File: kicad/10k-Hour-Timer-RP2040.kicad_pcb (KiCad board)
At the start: 2 copper layers, 2 parts, among them J1 USB_C_Receptacle_USB2.0_16P, J2 Conn_01x03_MountingPin

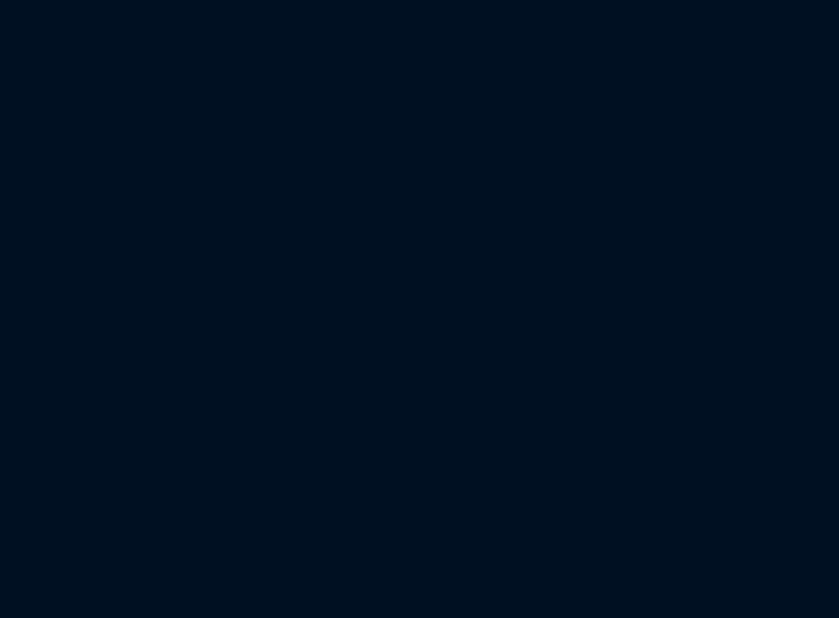
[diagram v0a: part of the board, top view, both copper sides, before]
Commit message: 3d model imports
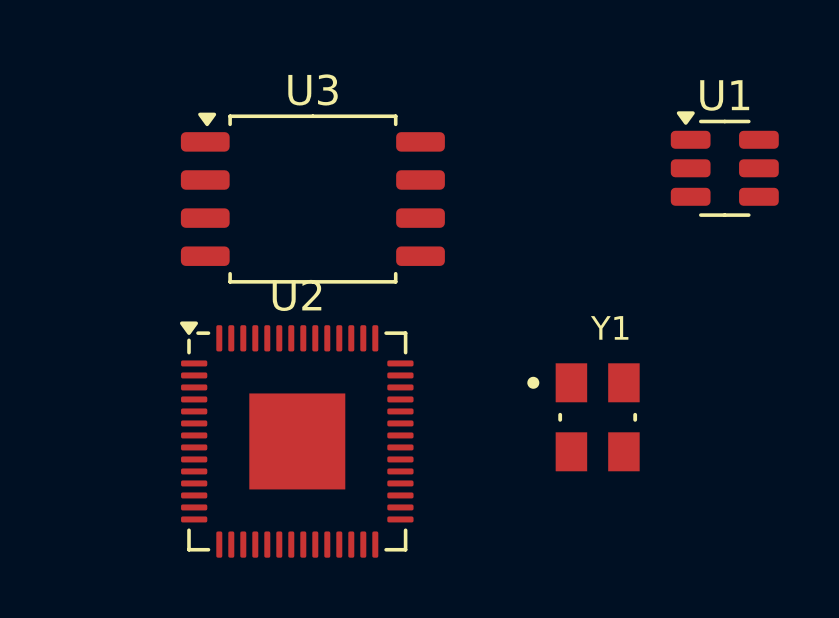
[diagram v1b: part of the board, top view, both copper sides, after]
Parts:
- added U1: USBLC6-2SC6, Package_TO_SOT_SMD:SOT-23-6, F.Cu at (133.9, 34.0)
- added U2: RP2040, Package_DFN_QFN:QFN-56-1EP_7x7mm_P0.4mm_EP3.2x3.2mm, F.Cu at (119.6, 43.2)
- added U3: W25Q128JVS, Package_SO:SOIC-8_5.3x5.3mm_P1.27mm, F.Cu at (120.1, 35.1)
- added Y1: ABM8-272-T3, project footprints:XTAL_ABM8-272-T3, F.Cu at (129.6, 42.4)
- J1: footprint Connector_USB:USB_C_Receptacle_JAE_DX07S016JA1R1500 -> project footprints:USB_C_Receptacle_JAE_DX07S016JA1R1500
- J2: footprint Connector_JST:JST_SH_SM03B-SRSS-TB_1x03-1MP_P1.00mm_Horizontal -> project footprints:JST_SH_SM03B-SRSS-TB_1x03-1MP_P1.00mm_Horizontal
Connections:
- net Net-(J1-VBUS-PadA4) renamed /01-04-Power-DCDC-Charger-Battery/5V_USB
- J1 pad A1: Net-(J1-GND-PadA1) -> GND
- J1 pad A12: Net-(J1-GND-PadA1) -> GND
- J1 pad A5: unconnected-(J1-CC1-PadA5) -> Net-(J1-CC1)
- J1 pad A6: unconnected-(J1-D+-PadA6) -> /USB_In_D+
- J1 pad A7: unconnected-(J1-D--PadA7) -> /USB_In_D-
- J1 pad B1: Net-(J1-GND-PadA1) -> GND
- J1 pad B12: Net-(J1-GND-PadA1) -> GND
- J1 pad B5: unconnected-(J1-CC2-PadB5) -> Net-(J1-CC2)
- J1 pad B6: unconnected-(J1-D+-PadB6) -> /USB_In_D+
- J1 pad B7: unconnected-(J1-D--PadB7) -> /USB_In_D-
- J1 pad S1: unconnected-(J1-SHIELD-PadS1) -> Net-(J1-SHIELD)
- J2 pad 1: unconnected-(J2-Pin_1-Pad1) -> /SWCK_UART_Rx
- J2 pad 2: unconnected-(J2-Pin_2-Pad2) -> GND
- J2 pad 3: unconnected-(J2-Pin_3-Pad3) -> /SWD_UART_Tx

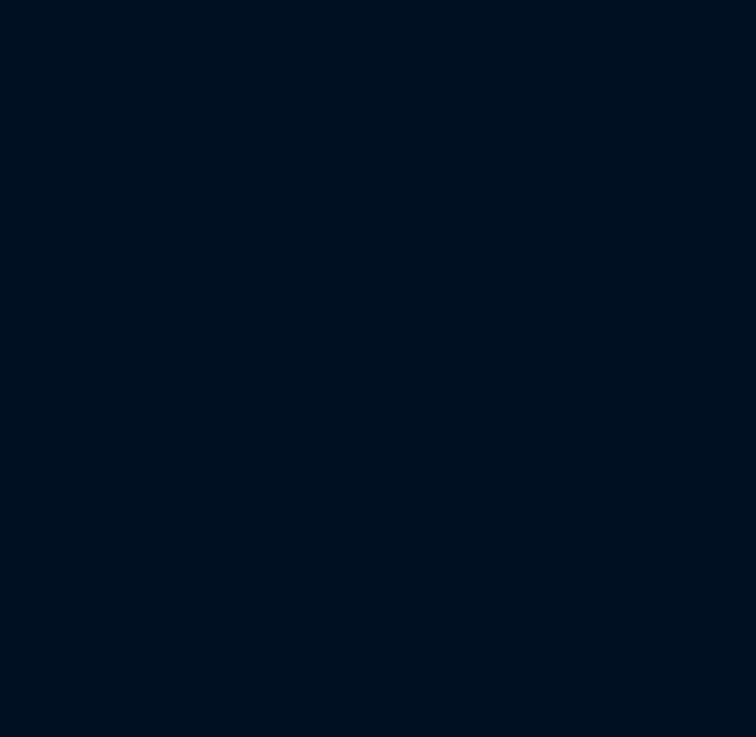
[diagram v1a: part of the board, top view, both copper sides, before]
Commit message: added charger and power mux
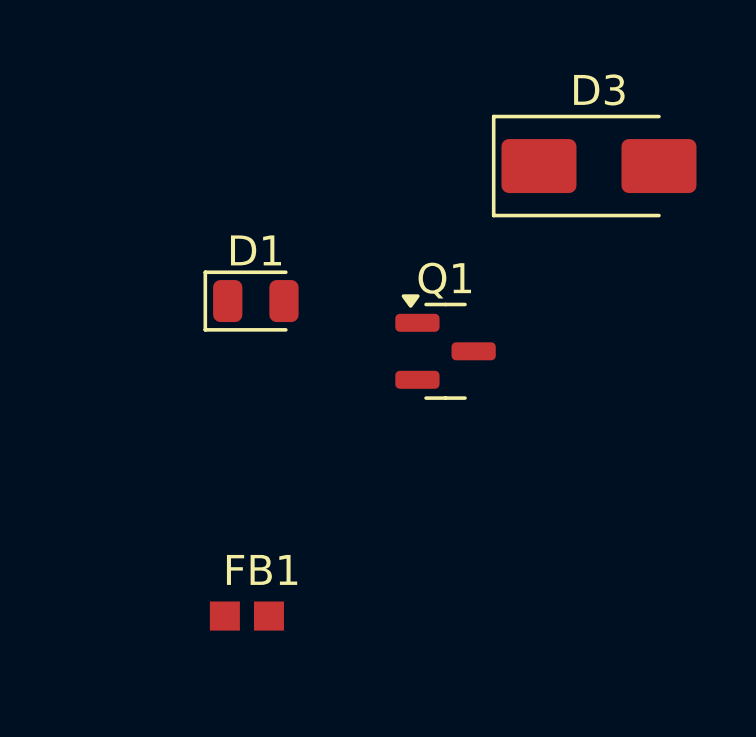
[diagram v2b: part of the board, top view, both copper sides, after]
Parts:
- added D1: LED, LED_SMD:LED_0805_2012Metric, F.Cu at (154.6, 34.5)
- added D3: SS14, Diode_SMD:D_SMA, F.Cu at (166.0, 30.0)
- added FB1: BLM18SP221SN1D, project footprints:BLM18SP221SN1D_BEADC1608X95N, F.Cu at (154.3, 45.0)
- added Q1: PMOS, Package_TO_SOT_SMD:SOT-23, F.Cu at (160.9, 36.2)
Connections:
- net /01-04-Power-DCDC-Charger-Battery/5V_USB renamed Net-(U1-VBUS)

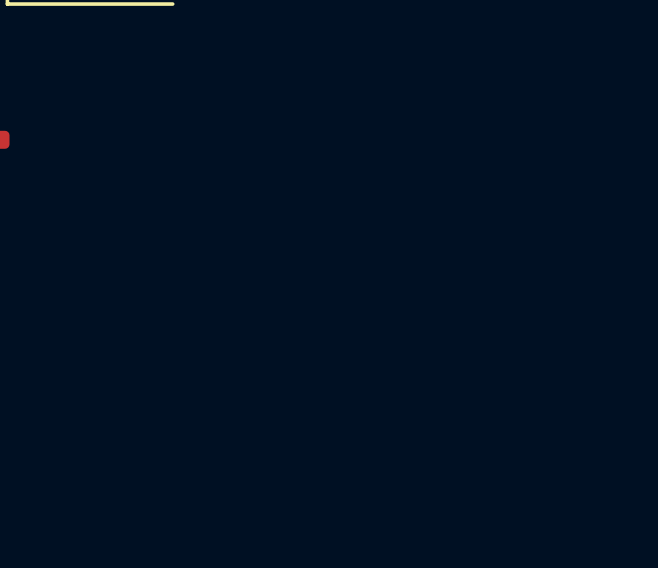
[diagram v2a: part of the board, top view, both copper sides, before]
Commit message: battery charger and protection
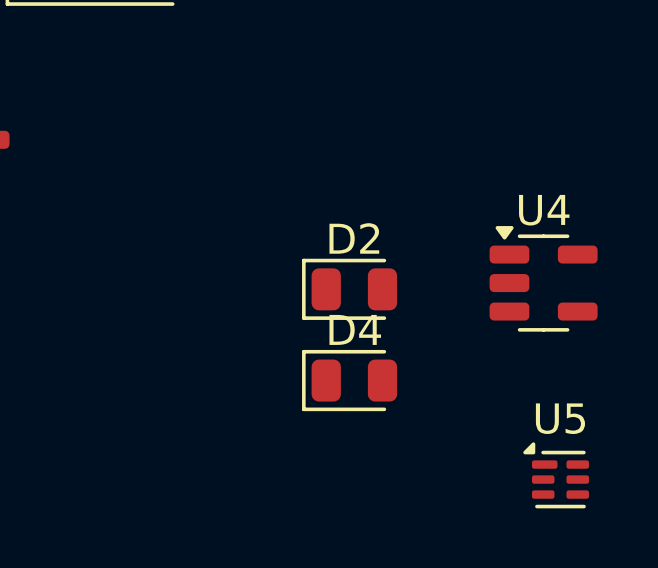
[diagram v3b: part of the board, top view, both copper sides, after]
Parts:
- added D2: BATT, LED_SMD:LED_0805_2012Metric, F.Cu at (174.1, 41.2)
- added D4: CHG, LED_SMD:LED_0805_2012Metric, F.Cu at (174.1, 44.2)
- added U4: MCP73831-2-OT, Package_TO_SOT_SMD:SOT-23-5, F.Cu at (180.4, 41.0)
- added U5: BQ29700DSER, Package_SON:WSON-6_1.5x1.5mm_P0.5mm, F.Cu at (180.9, 47.5)
- D1: value LED -> 5V
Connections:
- D3 pad 2: Net-(D3-A) -> /01-04-Power-DCDC-Charger-Battery/5V_USB
- Q1 pad 2: Net-(D3-A) -> /01-04-Power-DCDC-Charger-Battery/5V_USB

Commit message: dc dc start
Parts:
- added C7: 6.8p, Capacitor_SMD:C_0603_1608Metric_Pad1.08x0.95mm_HandSolder, F.Cu at (62.6, 80.5)
- added J3: S2B-PH-K-S_LF__SN_, Connector_JST:JST_PH_S2B-PH-K_1x02_P2.00mm_Horizontal, F.Cu at (55.5, 67.8)
- added L1: 2.2u, project footprints:IND_SDER041H-2R2MS, F.Cu at (106.5, 72.5)
- added Q2: AO3400A, Package_TO_SOT_SMD:SOT-23, F.Cu at (62.9, 72.4)
- added Q3: AO3400A, Package_TO_SOT_SMD:SOT-23, F.Cu at (62.9, 77.0)
- added U6: TLV62568DBV, Package_TO_SOT_SMD:SOT-23-5, F.Cu at (63.0, 67.8)
- J2: value Conn_01x03_MountingPin -> JST_SH_SM03B
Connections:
- net /01-04-Power-DCDC-Charger-Battery/+BATT renamed /01-04-Power-DCDC-Charger-Battery/Vbatt
- net /01-04-Power-DCDC-Charger-Battery/VBATT_VBUS renamed /01-04-Power-DCDC-Charger-Battery/Vbatt_Vbus
- J2 pad MP: unconnected-(J2-MountPin-PadMP) -> GND
- U5 pad 2: unconnected-(U5-Cout-Pad2) -> Net-(Q3-G)
- U5 pad 3: unconnected-(U5-Dout-Pad3) -> Net-(Q2-G)
- U5 pad 4: unconnected-(U5-VSS-Pad4) -> /01-04-Power-DCDC-Charger-Battery/Batt-
- U5 pad 5: unconnected-(U5-BAT-Pad5) -> Net-(U5-BAT)
- U5 pad 6: unconnected-(U5-V--Pad6) -> Net-(U5-V-)

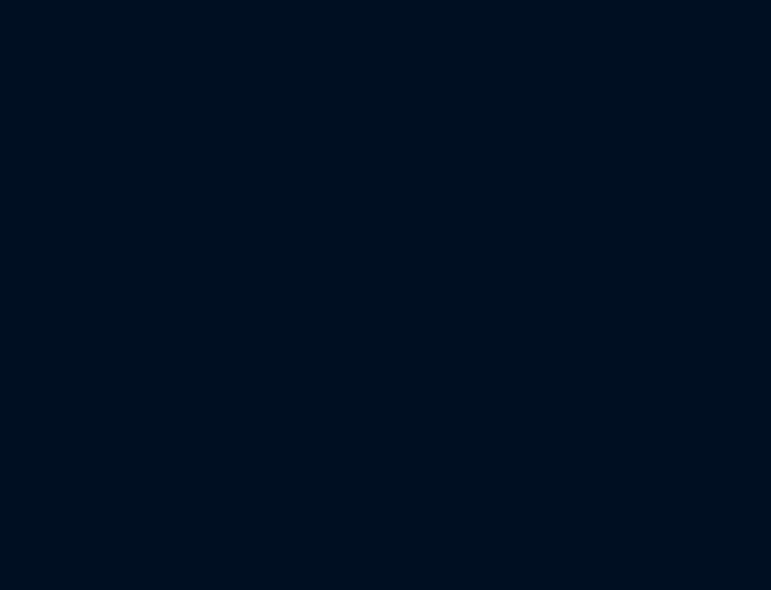
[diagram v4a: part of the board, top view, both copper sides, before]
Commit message: dcdc enable and swd
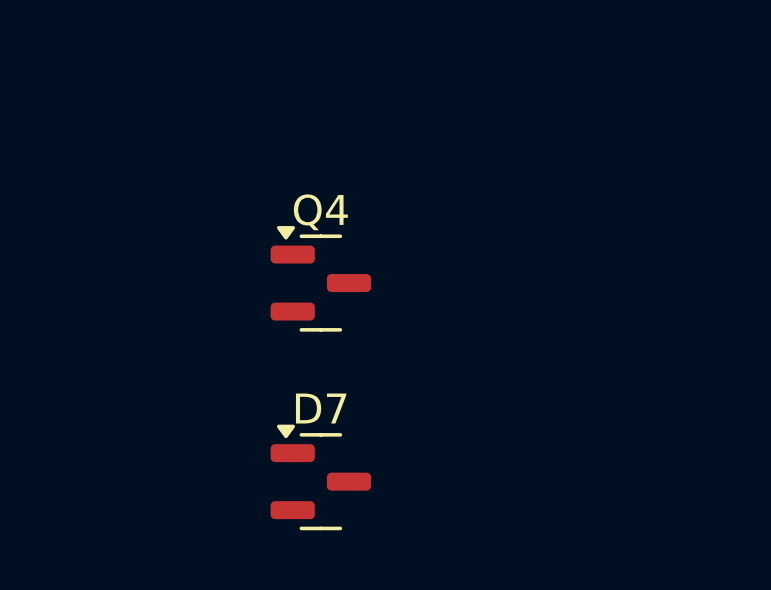
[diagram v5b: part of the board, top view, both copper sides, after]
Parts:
- added D7: BAT54C, Package_TO_SOT_SMD:SOT-23, F.Cu at (62.1, 108.0)
- added Q4: AO3400A, Package_TO_SOT_SMD:SOT-23, F.Cu at (62.1, 101.4)
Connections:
- net /SWCK_UART_Rx renamed /SWCLK
- net /SWD_UART_Tx renamed /SWDIO
- net Net-(C6-Pad1) renamed 3V3
- D3 pad 1: /01-04-Power-DCDC-Charger-Battery/Vbatt_Vbus -> Vbatt_Vbus
- Q1 pad 3: /01-04-Power-DCDC-Charger-Battery/Vbatt_Vbus -> Vbatt_Vbus
- U2 pad 24: unconnected-(U2-SWCLK-Pad24) -> Net-(U2-SWCLK)
- U2 pad 25: unconnected-(U2-SWD-Pad25) -> Net-(U2-SWD)
- U2 pad 46: unconnected-(U2-USB_DM-Pad46) -> Net-(U2-USB_DM)
- U2 pad 47: unconnected-(U2-USB_DP-Pad47) -> Net-(U2-USB_DP)
- U6 pad 1: unconnected-(U6-EN-Pad1) -> Net-(JP2-A)
- U6 pad 4: Net-(U6-VIN) -> Vbatt_Vbus

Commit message: mcu periphs
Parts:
- added C9: 6.8p, Capacitor_SMD:C_0603_1608Metric_Pad1.08x0.95mm_HandSolder, F.Cu at (118.3, 94.9)
- added D5: CHG, LED_SMD:LED_0805_2012Metric, F.Cu at (118.4, 92.1)
- added Q5: AO3400A, Package_TO_SOT_SMD:SOT-23, F.Cu at (125.1, 93.0)
- C7: value 6.8p -> 22u
- D1: value 5V -> BATT
- D2: value BATT -> 5V
- D4: value CHG -> BAT54C; footprint LED_SMD:LED_0805_2012Metric -> Package_TO_SOT_SMD:SOT-23
- J1: value USB_C_Receptacle_USB2.0_16P -> JST_SH_SM03B; footprint project footprints:USB_C_Receptacle_JAE_DX07S016JA1R1500 -> project footprints:JST_SH_SM03B-SRSS-TB_1x03-1MP_P1.00mm_Horizontal
- J2: value JST_SH_SM03B -> USB_C_Receptacle_USB2.0_16P; footprint project footprints:JST_SH_SM03B-SRSS-TB_1x03-1MP_P1.00mm_Horizontal -> project footprints:USB_C_Receptacle_JAE_DX07S016JA1R1500
- U2: value RP2040 -> BQ29700DSER; footprint Package_DFN_QFN:QFN-56-1EP_7x7mm_P0.4mm_EP3.2x3.2mm -> Package_SON:WSON-6_1.5x1.5mm_P0.5mm
- U3: value W25Q128JVS -> MCP73831-2-OT; footprint Package_SO:SOIC-8_5.3x5.3mm_P1.27mm -> Package_TO_SOT_SMD:SOT-23-5
- U4: value MCP73831-2-OT -> TLV62568DBV
- U5: value BQ29700DSER -> W25Q128JVS; footprint Package_SON:WSON-6_1.5x1.5mm_P0.5mm -> Package_SO:SOIC-8_5.3x5.3mm_P1.27mm
- U6: value TLV62568DBV -> RP2040; footprint Package_TO_SOT_SMD:SOT-23-5 -> Package_DFN_QFN:QFN-56-1EP_7x7mm_P0.4mm_EP3.2x3.2mm
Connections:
- net /05-07_MCU-LED-Driver-Displays/BSENSE_GPIO renamed Net-(Q4-D)
- net Net-(D4-K) renamed /01-04-Power-DCDC-Charger-Battery/BTN_PWR
- C7 pad 2: Net-(U6-FB) -> GND
- D1 pad 2: /01-04-Power-DCDC-Charger-Battery/5V_USB -> /01-04-Power-DCDC-Charger-Battery/Vbatt
- D2 pad 2: /01-04-Power-DCDC-Charger-Battery/Vbatt -> /01-04-Power-DCDC-Charger-Battery/5V_USB
- D4 pad 2: /01-04-Power-DCDC-Charger-Battery/5V_USB -> Net-(D4-Pad2)
- L1 pad 1: Net-(U6-SW) -> Net-(U4-SW)
- Q2 pad 2: /01-04-Power-DCDC-Charger-Battery/Batt- -> GND
- Q3 pad 2: GND -> /01-04-Power-DCDC-Charger-Battery/Batt-
- Q4 pad 1: /05-07_MCU-LED-Driver-Displays/BSENSE_Gate -> 3V3
- Q4 pad 2: GND -> /05-07_MCU-LED-Driver-Displays/ADC1
- U2 pad 1: Net-(U2-IOVDD-Pad1) -> unconnected-(U2-NC-Pad1)
- U2 pad 2: unconnected-(U2-GPIO0-Pad2) -> Net-(Q2-G)
- U2 pad 3: unconnected-(U2-GPIO1-Pad3) -> Net-(Q3-G)
- U2 pad 4: unconnected-(U2-GPIO2-Pad4) -> /01-04-Power-DCDC-Charger-Battery/Batt-
- U2 pad 5: unconnected-(U2-GPIO3-Pad5) -> Net-(U2-BAT)
- U2 pad 6: unconnected-(U2-GPIO4-Pad6) -> Net-(U2-V-)
- U3 pad 1: unconnected-(U3-~{CS}-Pad1) -> Net-(U3-STAT)
- U3 pad 2: unconnected-(U3-DO/IO_{1}-Pad2) -> GND
- U3 pad 3: unconnected-(U3-~{WP}/IO_{2}-Pad3) -> /01-04-Power-DCDC-Charger-Battery/Vbatt
- U3 pad 4: unconnected-(U3-GND-Pad4) -> /01-04-Power-DCDC-Charger-Battery/5V_USB
- U3 pad 5: unconnected-(U3-DI/IO_{0}-Pad5) -> Net-(U3-PROG)
- U4 pad 1: Net-(U4-STAT) -> Net-(JP2-A)
- U4 pad 3: /01-04-Power-DCDC-Charger-Battery/Vbatt -> Net-(U4-SW)
- U4 pad 4: /01-04-Power-DCDC-Charger-Battery/5V_USB -> Vbatt_Vbus
- U5 pad 1: unconnected-(U5-NC-Pad1) -> /05-07_MCU-LED-Driver-Displays/QSPI_SS
- U5 pad 2: Net-(Q3-G) -> /05-07_MCU-LED-Driver-Displays/QSPI_SD1
- U5 pad 3: Net-(Q2-G) -> /05-07_MCU-LED-Driver-Displays/QSPI_SD2
- U5 pad 4: /01-04-Power-DCDC-Charger-Battery/Batt- -> GND
- U5 pad 5: Net-(U5-BAT) -> /05-07_MCU-LED-Driver-Displays/QSPI_SD0
- U5 pad 6: Net-(U5-V-) -> /05-07_MCU-LED-Driver-Displays/QSPI_CLK
- U6 pad 1: Net-(JP2-A) -> 3V3
- U6 pad 2: GND -> /05-07_MCU-LED-Driver-Displays/UART0_Tx
- U6 pad 3: Net-(U6-SW) -> /05-07_MCU-LED-Driver-Displays/UART0_Rx
- U6 pad 4: Vbatt_Vbus -> unconnected-(U6-GPIO2-Pad4)
- U6 pad 5: Net-(U6-FB) -> unconnected-(U6-GPIO3-Pad5)

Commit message: DR  ✅ SYS-01-Power-Mux
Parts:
- added D6: BAT54C, Package_TO_SOT_SMD:SOT-23, F.Cu at (255.6, 52.3)
- added JP1: SolderJumper_2_Open, Jumper:SolderJumper-2_P1.3mm_Open_RoundedPad1.0x1.5mm, F.Cu at (258.9, 31.0)
- added JP10: SolderJumper_2_Bridged, Jumper:SolderJumper-2_P1.3mm_Bridged_RoundedPad1.0x1.5mm, F.Cu at (263.2, 11.2)
- added JP11: SolderJumper_2_Bridged, Jumper:SolderJumper-2_P1.3mm_Bridged_RoundedPad1.0x1.5mm, F.Cu at (263.2, 14.8)
- added JP12: SolderJumper_2_Bridged, Jumper:SolderJumper-2_P1.3mm_Bridged_RoundedPad1.0x1.5mm, F.Cu at (263.2, 18.4)
- added JP13: SolderJumper_2_Bridged, Jumper:SolderJumper-2_P1.3mm_Bridged_RoundedPad1.0x1.5mm, F.Cu at (256.6, 122.0)
- added JP14: SolderJumper_2_Open, Jumper:SolderJumper-2_P1.3mm_Open_RoundedPad1.0x1.5mm, F.Cu at (256.6, 125.5)
- added JP15: SolderJumper_2_Bridged, Jumper:SolderJumper-2_P1.3mm_Bridged_RoundedPad1.0x1.5mm, F.Cu at (256.6, 129.1)
- added JP16: SolderJumper_2_Bridged, Jumper:SolderJumper-2_P1.3mm_Bridged_RoundedPad1.0x1.5mm, F.Cu at (256.6, 132.7)
- added JP2: SolderJumper_2_Bridged, Jumper:SolderJumper-2_P1.3mm_Bridged_RoundedPad1.0x1.5mm, F.Cu at (69.2, 29.0)
- added JP3: SolderJumper_2_Open, Jumper:SolderJumper-2_P1.3mm_Open_RoundedPad1.0x1.5mm, F.Cu at (69.2, 32.5)
- added JP4: SolderJumper_2_Bridged, Jumper:SolderJumper-2_P1.3mm_Bridged_RoundedPad1.0x1.5mm, F.Cu at (69.0, 37.0)
- added JP5: SolderJumper_2_Open, Jumper:SolderJumper-2_P1.3mm_Open_RoundedPad1.0x1.5mm, F.Cu at (68.9, 41.5)
- added JP6: SolderJumper_2_Open, Jumper:SolderJumper-2_P1.3mm_Open_RoundedPad1.0x1.5mm, F.Cu at (68.9, 45.0)
- added JP7: SolderJumper_2_Bridged, Jumper:SolderJumper-2_P1.3mm_Bridged_RoundedPad1.0x1.5mm, F.Cu at (258.9, 18.4)
- added JP8: SolderJumper_2_Open, Jumper:SolderJumper-2_P1.3mm_Open_RoundedPad1.0x1.5mm, F.Cu at (258.9, 21.9)
- added JP9: SolderJumper_2_Bridged, Jumper:SolderJumper-2_P1.3mm_Bridged_RoundedPad1.0x1.5mm, F.Cu at (258.9, 25.4)
- added R1: 5K1, Resistor_SMD:R_0805_2012Metric_Pad1.20x1.40mm_HandSolder, F.Cu at (257.8, 68.3)
- added R10: 2.2K, Resistor_SMD:R_0805_2012Metric_Pad1.20x1.40mm_HandSolder, F.Cu at (246.2, 71.3)
- added R11: 5.1M, Resistor_SMD:R_0805_2012Metric_Pad1.20x1.40mm_HandSolder, F.Cu at (246.2, 74.2)
- added R12: 5.1M, Resistor_SMD:R_0805_2012Metric_Pad1.20x1.40mm_HandSolder, F.Cu at (246.2, 77.2)
- added R13: 1K, Resistor_SMD:R_0805_2012Metric_Pad1.20x1.40mm_HandSolder, F.Cu at (246.2, 80.2)
- added R14: 100K, Resistor_SMD:R_0805_2012Metric_Pad1.20x1.40mm_HandSolder, F.Cu at (251.0, 68.3)
- added R15: 200K, Resistor_SMD:R_0805_2012Metric_Pad1.20x1.40mm_HandSolder, F.Cu at (251.0, 71.3)
- added R16: 44.2K, Resistor_SMD:R_0805_2012Metric_Pad1.20x1.40mm_HandSolder, F.Cu at (251.0, 74.2)
- added R17: 10K, Resistor_SMD:R_0805_2012Metric_Pad1.20x1.40mm_HandSolder, F.Cu at (251.0, 77.2)
- added R18: 10K, Resistor_SMD:R_0805_2012Metric_Pad1.20x1.40mm_HandSolder, F.Cu at (241.5, 45.7)
- added R19: 10K, Resistor_SMD:R_0805_2012Metric_Pad1.20x1.40mm_HandSolder, F.Cu at (241.5, 48.6)
- added R2: 5K1, Resistor_SMD:R_0805_2012Metric_Pad1.20x1.40mm_HandSolder, F.Cu at (257.8, 71.3)
- added R20: 1K, Resistor_SMD:R_0805_2012Metric_Pad1.20x1.40mm_HandSolder, F.Cu at (241.5, 51.6)
- added R21: 1K, Resistor_SMD:R_0805_2012Metric_Pad1.20x1.40mm_HandSolder, F.Cu at (241.5, 54.5)
- added R22: 1K, Resistor_SMD:R_0805_2012Metric_Pad1.20x1.40mm_HandSolder, F.Cu at (241.5, 57.5)
- added R23: 1M, Resistor_SMD:R_0805_2012Metric_Pad1.20x1.40mm_HandSolder, F.Cu at (241.5, 60.5)
- added R24: 27, Resistor_SMD:R_0805_2012Metric_Pad1.20x1.40mm_HandSolder, F.Cu at (241.5, 63.4)
- added R25: 10K, Resistor_SMD:R_0805_2012Metric_Pad1.20x1.40mm_HandSolder, F.Cu at (246.2, 45.7)
- added R26: 27, Resistor_SMD:R_0805_2012Metric_Pad1.20x1.40mm_HandSolder, F.Cu at (246.2, 48.6)
- added R27: 100, Resistor_SMD:R_0805_2012Metric_Pad1.20x1.40mm_HandSolder, F.Cu at (246.2, 51.6)
- added R28: 100, Resistor_SMD:R_0805_2012Metric_Pad1.20x1.40mm_HandSolder, F.Cu at (246.2, 54.5)
- added R29: 1K, Resistor_SMD:R_0805_2012Metric_Pad1.20x1.40mm_HandSolder, F.Cu at (246.2, 57.5)
- added R3: 1K, Resistor_SMD:R_0805_2012Metric_Pad1.20x1.40mm_HandSolder, F.Cu at (53.0, 40.5)
- added R30: 1, Resistor_SMD:R_0805_2012Metric_Pad1.20x1.40mm_HandSolder, F.Cu at (246.2, 60.5)
- added R31: 10K, Resistor_SMD:R_0805_2012Metric_Pad1.20x1.40mm_HandSolder, F.Cu at (246.2, 63.4)
- added R32: 10K, Resistor_SMD:R_0805_2012Metric_Pad1.20x1.40mm_HandSolder, F.Cu at (251.0, 45.7)
- added R33: 1K, Resistor_SMD:R_0805_2012Metric_Pad1.20x1.40mm_HandSolder, F.Cu at (251.0, 48.6)
- added R34: 470, Resistor_SMD:R_0805_2012Metric_Pad1.20x1.40mm_HandSolder, F.Cu at (251.0, 51.6)
- added R35: 1K, Resistor_SMD:R_0805_2012Metric_Pad1.20x1.40mm_HandSolder, F.Cu at (251.0, 54.5)
- added R36: 10K, Resistor_SMD:R_0805_2012Metric_Pad1.20x1.40mm_HandSolder, F.Cu at (251.0, 57.5)
- added R37: 10K, Resistor_SMD:R_0805_2012Metric_Pad1.20x1.40mm_HandSolder, F.Cu at (251.0, 60.5)
- added R4: 10K, Resistor_SMD:R_0805_2012Metric_Pad1.20x1.40mm_HandSolder, F.Cu at (53.0, 43.5)
- added R5: 2K, Resistor_SMD:R_0805_2012Metric_Pad1.20x1.40mm_HandSolder, F.Cu at (47.0, 41.0)
- added R6: 2K, Resistor_SMD:R_0805_2012Metric_Pad1.20x1.40mm_HandSolder, F.Cu at (53.0, 34.0)
- added R7: 2K, Resistor_SMD:R_0805_2012Metric_Pad1.20x1.40mm_HandSolder, F.Cu at (167.6, 121.5)
- added R8: 0, Resistor_SMD:R_0805_2012Metric_Pad1.20x1.40mm_HandSolder, F.Cu at (53.0, 36.9)
- added R9: 330, Resistor_SMD:R_0805_2012Metric_Pad1.20x1.40mm_HandSolder, F.Cu at (246.2, 68.3)
- added TP1: TestPoint, project footprints:TestPoint_THTPad_D2.0mm_Drill1.0mm, F.Cu at (250.2, 104.2)
- added TP10: TestPoint, project footprints:TestPoint_THTPad_D2.0mm_Drill1.0mm, F.Cu at (259.5, 113.5)
- added TP11: TestPoint, project footprints:TestPoint_THTPad_D2.0mm_Drill1.0mm, F.Cu at (243.6, 92.9)
- added TP12: TestPoint, project footprints:TestPoint_THTPad_D2.0mm_Drill1.0mm, F.Cu at (243.6, 97.5)
- added TP13: TestPoint, project footprints:TestPoint_THTPad_D2.0mm_Drill1.0mm, F.Cu at (234.5, 106.0)
- added TP14: TestPoint, project footprints:TestPoint_THTPad_D2.0mm_Drill1.0mm, F.Cu at (250.2, 92.9)
- added TP15: TestPoint, project footprints:TestPoint_THTPad_D2.0mm_Drill1.0mm, F.Cu at (250.2, 97.5)
- added TP16: TestPoint, project footprints:TestPoint_THTPad_D2.0mm_Drill1.0mm, F.Cu at (254.8, 92.9)
- added TP17: TestPoint, project footprints:TestPoint_THTPad_D2.0mm_Drill1.0mm, F.Cu at (254.8, 97.5)
- added TP18: TestPoint, project footprints:TestPoint_THTPad_D2.0mm_Drill1.0mm, F.Cu at (259.5, 92.9)
- added TP19: TestPoint, project footprints:TestPoint_THTPad_D2.0mm_Drill1.0mm, F.Cu at (259.5, 97.5)
- added TP2: TestPoint, project footprints:TestPoint_THTPad_D2.0mm_Drill1.0mm, F.Cu at (250.2, 108.8)
- added TP20: TestPoint, project footprints:TestPoint_THTPad_D2.0mm_Drill1.0mm, F.Cu at (245.0, 105.5)
- added TP21: TestPoint, project footprints:TestPoint_THTPad_D2.0mm_Drill1.0mm, F.Cu at (246.0, 118.5)
- added TP3: TestPoint, project footprints:TestPoint_THTPad_D2.0mm_Drill1.0mm, F.Cu at (250.2, 113.5)
- added TP4: VBATT, project footprints:TestPoint_THTPad_D2.0mm_Drill1.0mm, F.Cu at (60.2, 30.5)
- added TP5: VBUS, project footprints:TestPoint_THTPad_D2.0mm_Drill1.0mm, F.Cu at (60.2, 36.0)
- added TP6: VSW, project footprints:TestPoint_THTPad_D2.0mm_Drill1.0mm, F.Cu at (60.7, 43.0)
- added TP7: TestPoint, project footprints:TestPoint_THTPad_D2.0mm_Drill1.0mm, F.Cu at (259.5, 104.2)
- added TP8: TestPoint, project footprints:TestPoint_THTPad_D2.0mm_Drill1.0mm, F.Cu at (259.5, 108.8)
- added TP9: TestPoint, project footprints:TestPoint_THTPad_D2.0mm_Drill1.0mm, F.Cu at (245.0, 112.5)
- added U7: RP2040, Package_DFN_QFN:QFN-56-1EP_7x7mm_P0.4mm_EP3.2x3.2mm, F.Cu at (257.6, 47.6)
- added Y2: ABM8-272-T3, project footprints:XTAL_ABM8-272-T3, F.Cu at (168.0, 115.5)
- C7: value 22u -> 470n
- D3: value SS14 -> SOD-323; footprint Diode_SMD:D_SMA -> Diode_SMD:D_SOD-323_HandSoldering
- D4: value BAT54C -> SS14; footprint Package_TO_SOT_SMD:SOT-23 -> Diode_SMD:D_SMA
- D7: value BAT54C -> RED; footprint Package_TO_SOT_SMD:SOT-23 -> LED_SMD:LED_0805_2012Metric
- U2: value BQ29700DSER -> MCP73831-2-OT; footprint Package_SON:WSON-6_1.5x1.5mm_P0.5mm -> Package_TO_SOT_SMD:SOT-23-5
- U3: value MCP73831-2-OT -> BQ29700DSER; footprint Package_TO_SOT_SMD:SOT-23-5 -> Package_SON:WSON-6_1.5x1.5mm_P0.5mm
- U6: value RP2040 -> PCF8523T; footprint Package_DFN_QFN:QFN-56-1EP_7x7mm_P0.4mm_EP3.2x3.2mm -> Package_SO:SOIC-8_3.9x4.9mm_P1.27mm
- Y1: value ABM8-272-T3 -> ABS07AIG-32.768KHZ-7-T
- moved D4 136.3 mm to (38.0, 35.5)
- moved D2 122.3 mm to (52.4, 28.0)
- moved D3 119.3 mm to (47.8, 45.5)
- moved Q1 114.9 mm to (45.9, 35.5)
- moved D1 102.8 mm to (52.6, 47.0)
- moved D7 79.1 mm to (45.2, 30.7)
- moved Q2 64.8 mm to (119.9, 103.1)
- moved Q3 64.8 mm to (119.9, 107.8)
- moved C7 64.8 mm to (119.7, 111.2)
- moved J3 64.8 mm to (112.5, 98.5)
- moved Q4 64.8 mm to (119.1, 132.1)
- moved U6 64.8 mm to (120.0, 98.5)
- moved D5 33.4 mm to (143.9, 113.6)
- moved FB1 33.4 mm to (179.8, 66.5)
- moved L1 33.4 mm to (132.0, 94.0)
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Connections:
- C7 pad 1: 3V3 -> Net-(JP8-A)
- D3 pad 1: Vbatt_Vbus -> /01-04-Power-DCDC-Charger-Battery/ADC1_VSW_In
- D3 pad 2: /01-04-Power-DCDC-Charger-Battery/5V_USB -> Net-(D3-A)
- D4 pad 1: /01-04-Power-DCDC-Charger-Battery/BTN_PWR -> /01-04-Power-DCDC-Charger-Battery/ADC1_VSW_In
- D7 pad 1: /05-07_MCU-LED-Driver-Displays/BSENSE_Gate -> GND
- Q1 pad 3: Vbatt_Vbus -> /01-04-Power-DCDC-Charger-Battery/ADC1_VSW_In
- U2 pad 1: unconnected-(U2-NC-Pad1) -> Net-(U2-STAT)
- U2 pad 2: Net-(Q2-G) -> GND
- U2 pad 3: Net-(Q3-G) -> /01-04-Power-DCDC-Charger-Battery/Vbatt
- U2 pad 4: /01-04-Power-DCDC-Charger-Battery/Batt- -> /01-04-Power-DCDC-Charger-Battery/5V_USB
- U3 pad 1: Net-(U3-STAT) -> unconnected-(U3-NC-Pad1)
- U3 pad 2: GND -> Net-(Q2-G)
- U3 pad 3: /01-04-Power-DCDC-Charger-Battery/Vbatt -> Net-(Q3-G)
- U3 pad 4: /01-04-Power-DCDC-Charger-Battery/5V_USB -> /01-04-Power-DCDC-Charger-Battery/Batt-
- U4 pad 1: Net-(JP2-A) -> Net-(JP7-A)
- U6 pad 1: 3V3 -> Net-(U6-OSCI)
- U6 pad 2: /05-07_MCU-LED-Driver-Displays/UART0_Tx -> Net-(U6-OSCO)
- U6 pad 3: /05-07_MCU-LED-Driver-Displays/UART0_Rx -> /01-04-Power-DCDC-Charger-Battery/Vbatt
- U6 pad 4: unconnected-(U6-GPIO2-Pad4) -> GND
- U6 pad 5: unconnected-(U6-GPIO3-Pad5) -> /05-07_MCU-LED-Driver-Displays/I2C_SDA
- U6 pad 6: unconnected-(U6-GPIO4-Pad6) -> /05-07_MCU-LED-Driver-Displays/I2C_SCL
- U6 pad 7: unconnected-(U6-GPIO5-Pad7) -> /05-07_MCU-LED-Driver-Displays/CLKOUT
- U6 pad 8: unconnected-(U6-GPIO6-Pad8) -> Net-(U6-VDD)
- Y1 pad 1: unconnected-(Y1-Pad1) -> Net-(U6-OSCO)
- Y1 pad 2: unconnected-(Y1-Pad2) -> Net-(U6-OSCI)
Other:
- board outline added: 245 x 173 mm
- board text added: "Power-Mux"
